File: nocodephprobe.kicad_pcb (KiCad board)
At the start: 2 copper layers, 76 x 80.9 mm, 30 parts, among them J1 RF1-01 BNC, J2 10K, Q1 2N7002, U1 LMV358a, U2 ICL7106CPL, U3 MCP1501T-10E/CHY, U4 VI-302-DP-RC-S

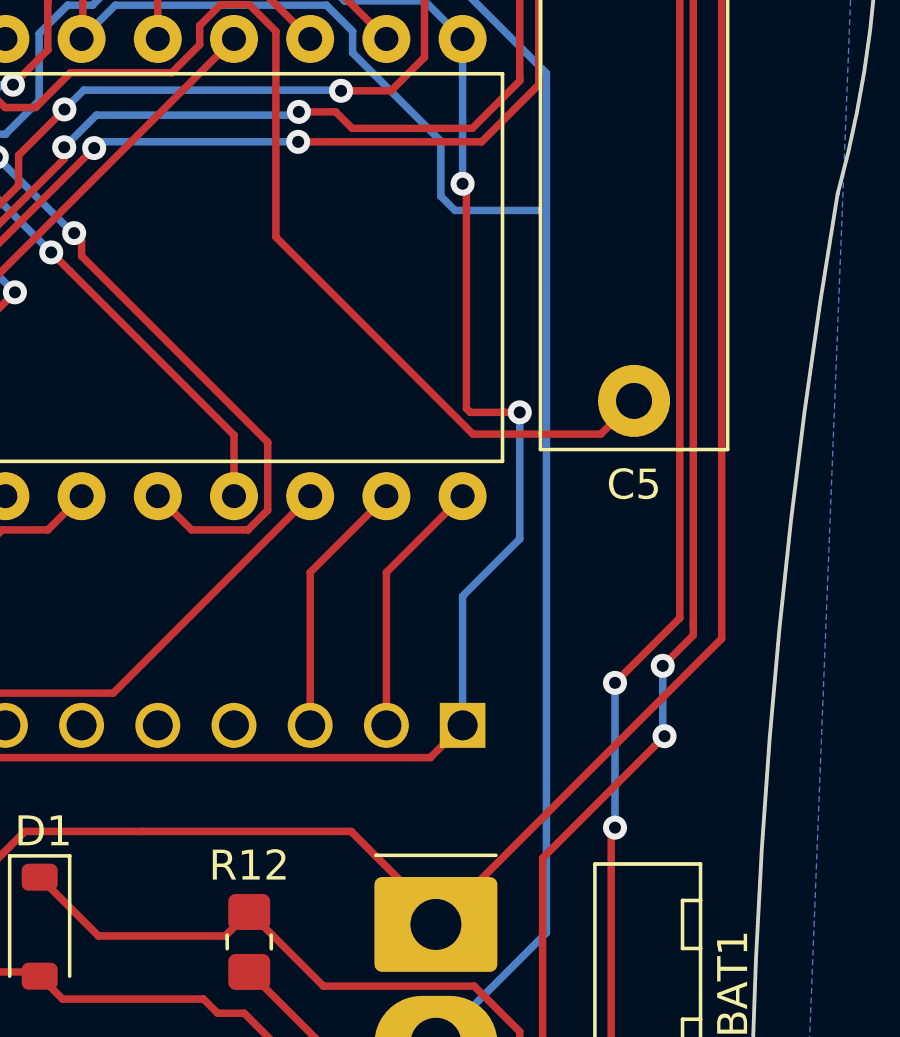
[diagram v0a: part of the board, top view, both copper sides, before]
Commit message: Add silkscreen labels to power nets
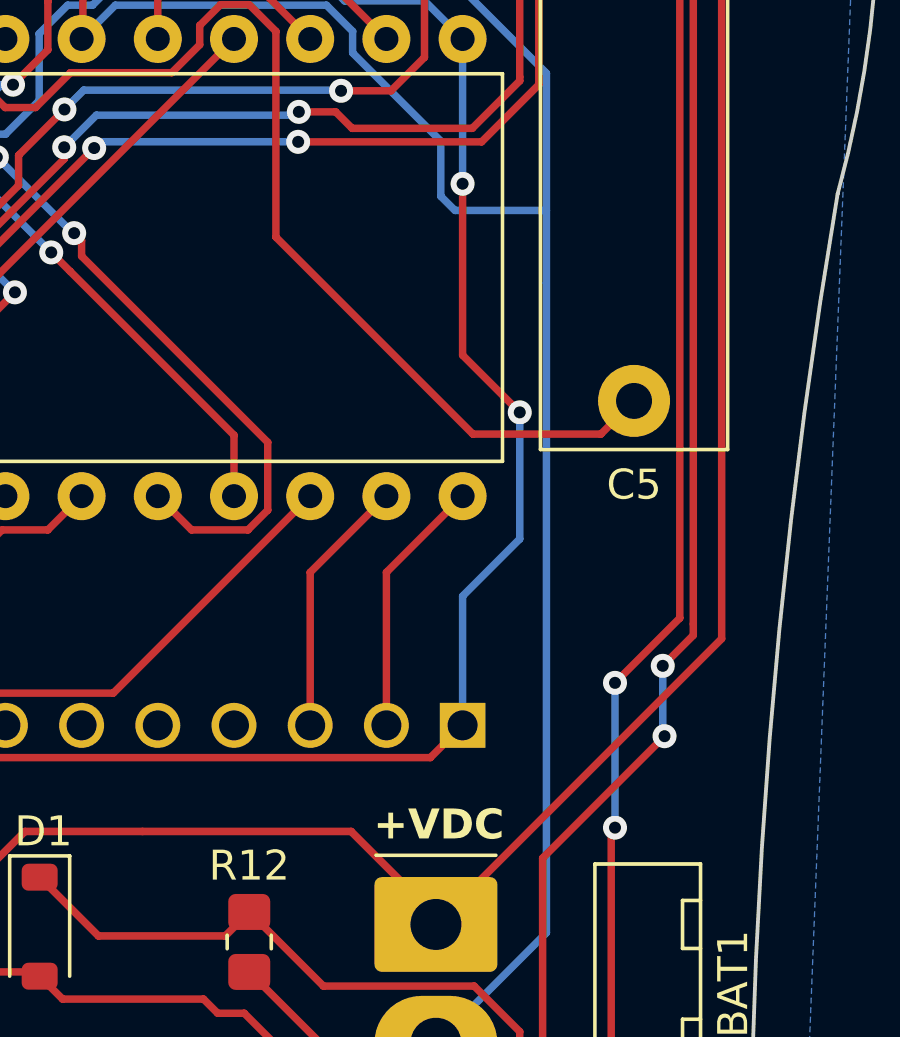
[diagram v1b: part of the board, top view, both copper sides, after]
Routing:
- net BP: track 126.9 -> 125.9 mm
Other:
- board text added: "+VDC"
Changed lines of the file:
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@@
     (effects (font (size 1.5 1.5) (thickness 0.3) bold) (justify left bottom))
+  )
+  (gr_text "+VDC" (at 169.75 104.75) (layer "F.SilkS")
+    (effects (font (size 1 1) (thickness 0.2) bold) (justify left bottom))
   )
   (segment (start 181.356 71.882) (end 181.356 97.969) (width 0.25) (layer "F.Cu") (net 1))
@@
   (segment (start 154.94 100.858) (end 153.563 102.235) (width 0.25) (layer "F.Cu") (net 13))
   (segment (start 153.563 102.235) (end 149.352 102.235) (width 0.25) (layer "F.Cu") (net 13))
+  (segment (start 172.72 82.804) (end 172.72 88.519) (width 0.25) (layer "F.Cu") (net 13))
   (segment (start 130.863297 71.681297) (end 142.504659 71.681297) (width 0.25) (layer "F.Cu") (net 13))
   (segment (start 172.72 100.858) (end 171.645 101.933) (width 0.25) (layer "F.Cu") (net 13))
-  (segment (start 172.847 90.297) (end 172.974 90.424) (width 0.25) (layer "F.Cu") (net 13))
   (segment (start 147.001183 102.383) (end 134.016 102.383) (width 0.25) (layer "F.Cu") (net 13))
   (segment (start 129.54 70.358) (end 130.863297 71.681297) (width 0.25) (layer "F.Cu") (net 13))
   (segment (start 127 70.358) (end 129.54 70.358) (width 0.25) (layer "F.Cu") (net 13))
   (segment (start 124.46 70.358) (end 127 70.358) (width 0.25) (layer "F.Cu") (net 13))
-  (segment (start 172.847 82.931) (end 172.847 90.297) (width 0.25) (layer "F.Cu") (net 13))
-  (segment (start 172.72 82.804) (end 172.847 82.931) (width 0.25) (layer "F.Cu") (net 13))
-  (segment (start 172.974 90.424) (end 174.625 90.424) (width 0.25) (layer "F.Cu") (net 13))
   (segment (start 147.183593 102.20059) (end 147.001183 102.383) (width 0.25) (layer "F.Cu") (net 13))
   (segment (start 133.5555 107.277) (end 133.5555 101.9225) (width 0.25) (layer "F.Cu") (net 13))
@@
   (segment (start 134.016 102.383) (end 133.5555 101.9225) (width 0.25) (layer "F.Cu") (net 13))
   (segment (start 133.5555 101.9225) (end 134.62 100.858) (width 0.25) (layer "F.Cu") (net 13))
+  (segment (start 172.72 88.519) (end 174.625 90.424) (width 0.25) (layer "F.Cu") (net 13))
   (via (at 172.72 82.804) (size 0.8) (drill 0.4) (layers "F.Cu" "B.Cu") (net 13))
   (via (at 149.352 102.235) (size 0.8) (drill 0.4) (layers "F.Cu" "B.Cu") (net 13))

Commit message: pcb: move trace away from edge
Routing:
- net Net-(D1-A): track 37.3 -> 34.3 mm
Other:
- board text added: "-VDC"
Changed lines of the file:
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@@
     (effects (font (size 1.5 1.5) (thickness 0.3) bold) (justify left bottom))
   )
-  (gr_text "+VDC" (at 169.75 104.75) (layer "F.SilkS")
+  (gr_text "-VDC" (at 169.5 115.25) (layer "F.SilkS")
+    (effects (font (size 1 1) (thickness 0.2) bold) (justify left bottom))
+  )
+  (gr_text "+VDC" (at 169.5 104.75) (layer "F.SilkS")
     (effects (font (size 1 1) (thickness 0.2) bold) (justify left bottom))
   )
@@
   (segment (start 123.19 68.834) (end 123.19 63.5) (width 0.25) (layer "F.Cu") (net 57))
   (segment (start 158.608 109.077) (end 158.623 109.092) (width 0.254) (layer "F.Cu") (net 58))
-  (segment (start 159.386 109.982) (end 164.084 109.982) (width 0.25) (layer "F.Cu") (net 58))
-  (segment (start 175.387 117.459) (end 171.231 117.459) (width 0.25) (layer "F.Cu") (net 58))
+  (segment (start 180.086 125.984) (end 175.387 121.285) (width 0.25) (layer "F.Cu") (net 58))
+  (segment (start 173.353604 117.459) (end 166.348604 110.454) (width 0.25) (layer "F.Cu") (net 58))
   (segment (start 155.448 109.077) (end 158.608 109.077) (width 0.25) (layer "F.Cu") (net 58))
-  (segment (start 170.622388 115.635612) (end 170.622388 116.850389) (width 0.25) (layer "F.Cu") (net 58))
-  (segment (start 170.622388 116.850389) (end 170.7135 116.9415) (width 0.25) (layer "F.Cu") (net 58))
-  (segment (start 171.231 117.459) (end 170.7135 116.9415) (width 0.25) (layer "F.Cu") (net 58))
+  (segment (start 164.084 109.982) (end 159.386 109.982) (width 0.25) (layer "F.Cu") (net 58))
   (segment (start 158.623 109.092) (end 158.623 109.219) (width 0.254) (layer "F.Cu") (net 58))
+  (segment (start 164.556 110.454) (end 164.084 109.982) (width 0.25) (layer "F.Cu") (net 58))
   (segment (start 179.755999 125.984) (end 180.086 125.984) (width 0.254) (layer "F.Cu") (net 58))
-  (segment (start 164.556 110.454) (end 165.440776 110.454) (width 0.25) (layer "F.Cu") (net 58))
-  (segment (start 164.084 109.982) (end 164.556 110.454) (width 0.25) (layer "F.Cu") (net 58))
-  (segment (start 158.623 109.219) (end 159.386 109.982) (width 0.25) (layer "F.Cu") (net 58))
-  (segment (start 165.440776 110.454) (end 170.622388 115.635612) (width 0.25) (layer "F.Cu") (net 58))
-  (segment (start 170.7135 116.9415) (end 179.755999 125.984) (width 0.25) (layer "F.Cu") (net 58))
+  (segment (start 159.386 109.982) (end 158.623 109.219) (width 0.25) (layer "F.Cu") (net 58))
+  (segment (start 175.387 117.459) (end 173.353604 117.459) (width 0.25) (layer "F.Cu") (net 58))
+  (segment (start 166.348604 110.454) (end 164.556 110.454) (width 0.25) (layer "F.Cu") (net 58))
+  (segment (start 175.387 121.285) (end 175.387 117.459) (width 0.25) (layer "F.Cu") (net 58))
   (zone (net 4) (net_name "GND") (layer "B.Cu") (hatch edge 0.5)
     (connect_pads (clearance 0.5))

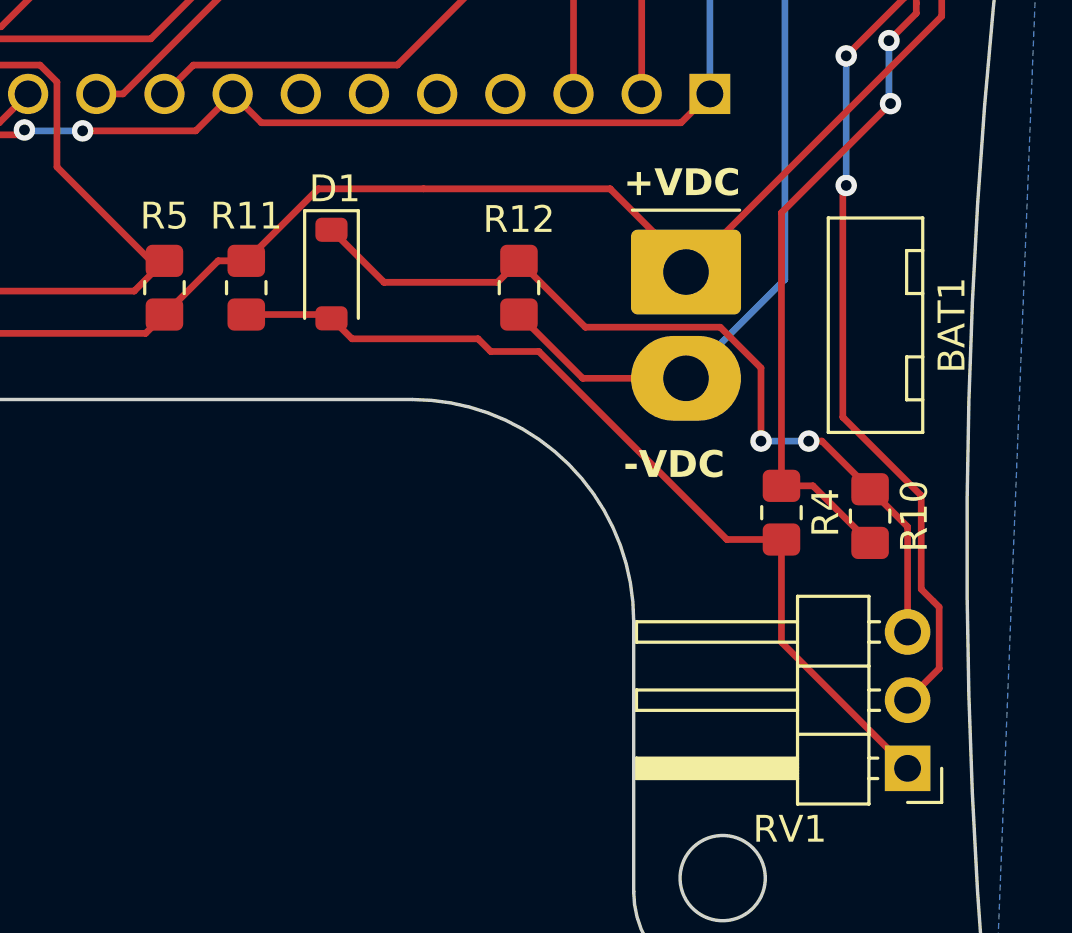
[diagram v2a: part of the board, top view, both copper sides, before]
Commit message: pcb: make d1 and r12 more compact
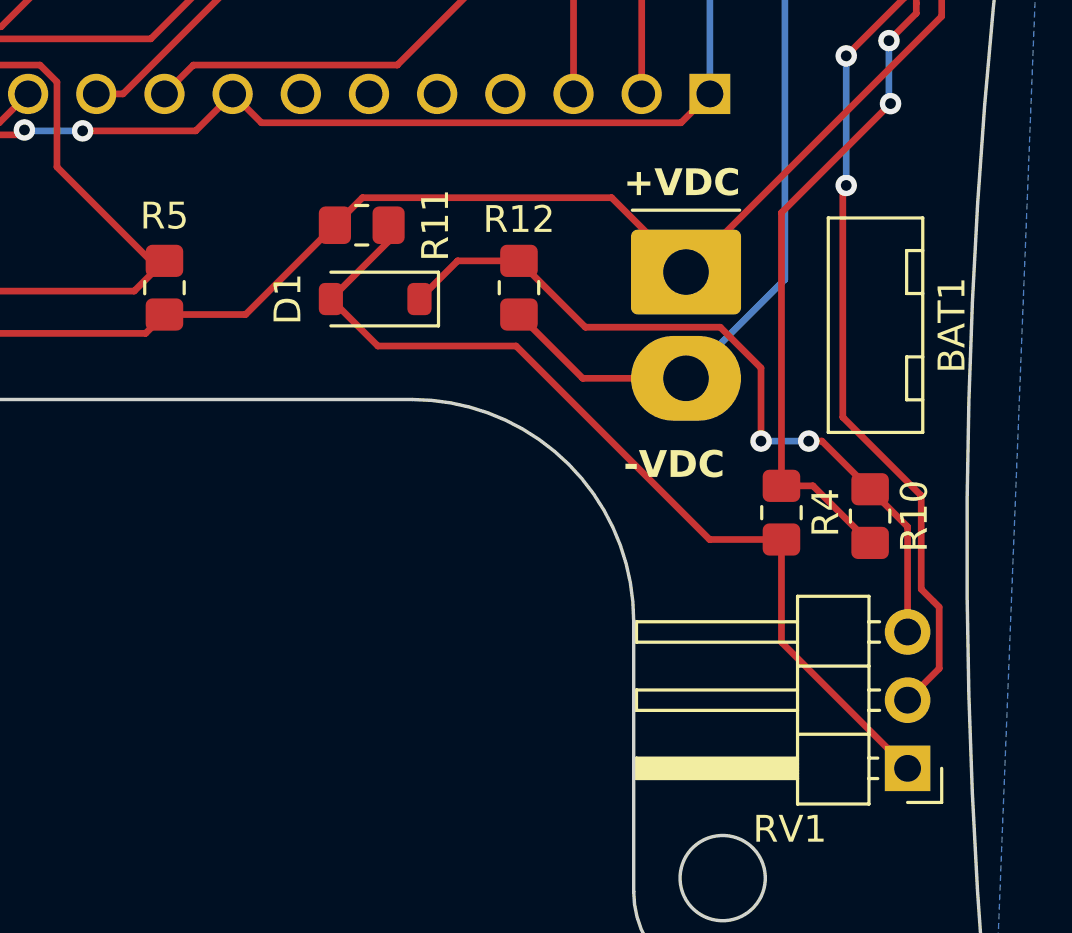
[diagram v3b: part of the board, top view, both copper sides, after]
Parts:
- moved R11 4.89 mm to (159.8, 105.8), turned to 180 degrees
- moved D1 1.87 mm to (160.2, 108.5), turned to 180 degrees
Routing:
- net Net-(D1-K): track 32.2 -> 28.4 mm
- net +VDC: track 131.7 -> 131.0 mm

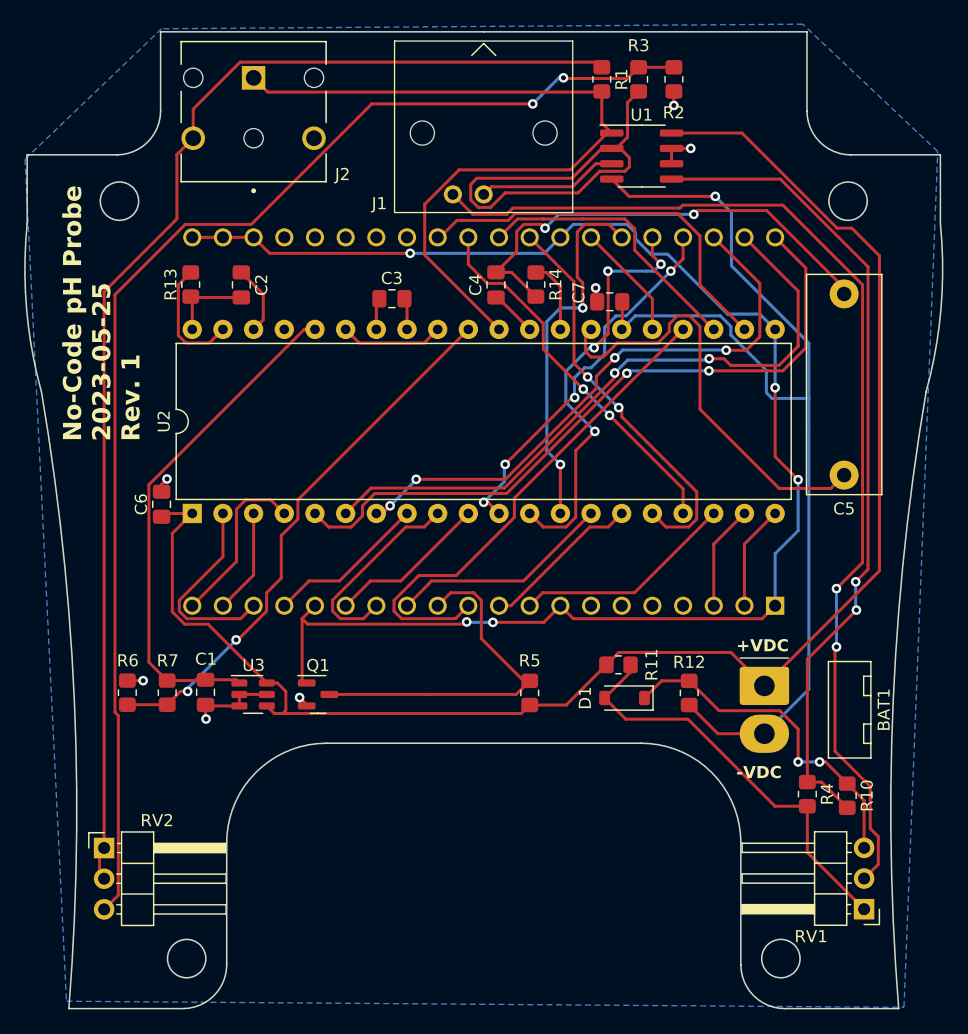
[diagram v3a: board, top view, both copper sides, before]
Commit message: pcb: move components away from edge and eliminate 2 vias
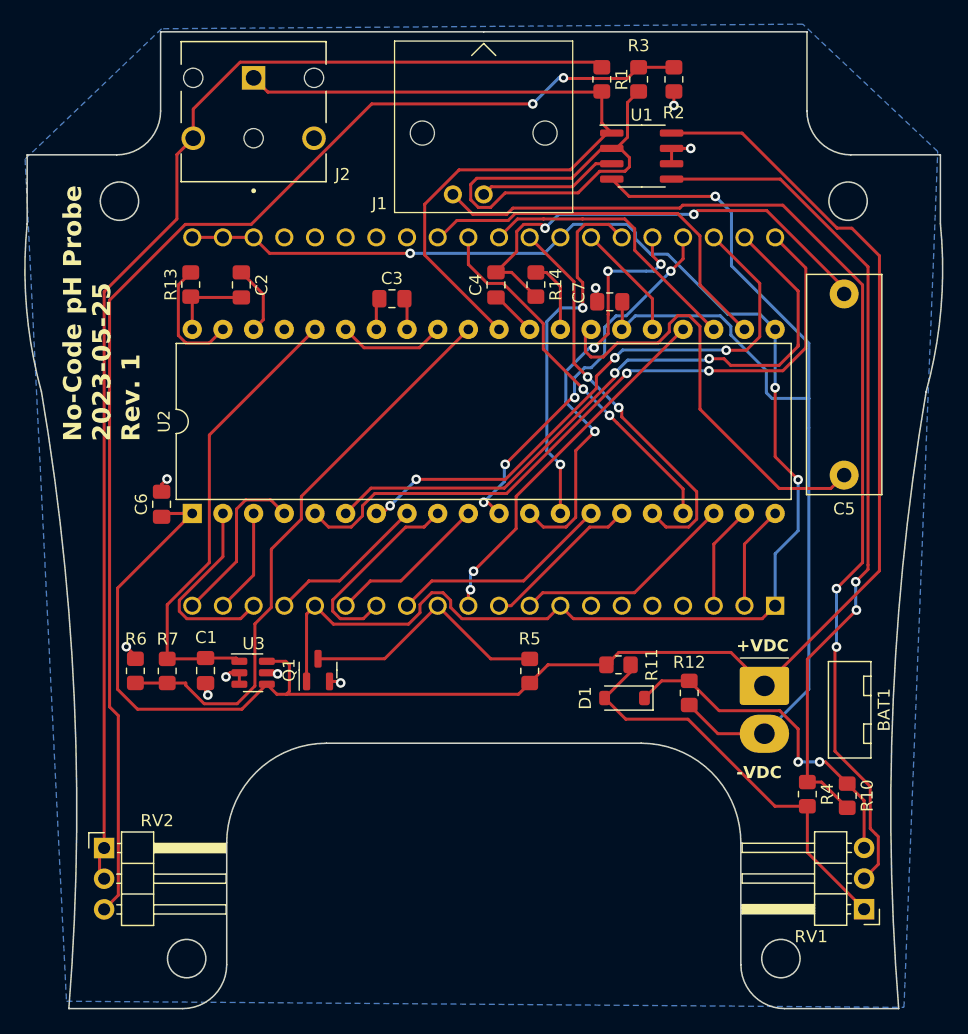
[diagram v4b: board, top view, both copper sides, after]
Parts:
- moved Q1 2.02 mm to (134.9, 106.2), turned to 90 degrees
- moved R6 1.92 mm to (119.8, 106.2)
- moved R5 1.82 mm to (152.4, 106.3)
- moved R7 1.80 mm to (122.4, 106.3)
- moved C1 1.80 mm to (125.6, 106.2)
- moved U3 1.80 mm to (129.5, 106.4)
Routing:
- net +VDC: track 131.0 -> 143.1 mm
- net Net-(U2-C3): track 41.9 -> 30.2 mm, vias 0 -> 2
- net DP: track 30.0 -> 21.2 mm
- net Vref: track 42.0 -> 38.5 mm
- net Voffset: track 45.1 -> 48.2 mm, vias 2 -> 0
- net GND: track 24.5 -> 21.8 mm, vias 7 -> 9
- net BP: track 125.9 -> 127.5 mm, vias 5 -> 3
